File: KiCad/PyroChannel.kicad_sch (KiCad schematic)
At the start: 5 parts, among them Q3 IRLML0030

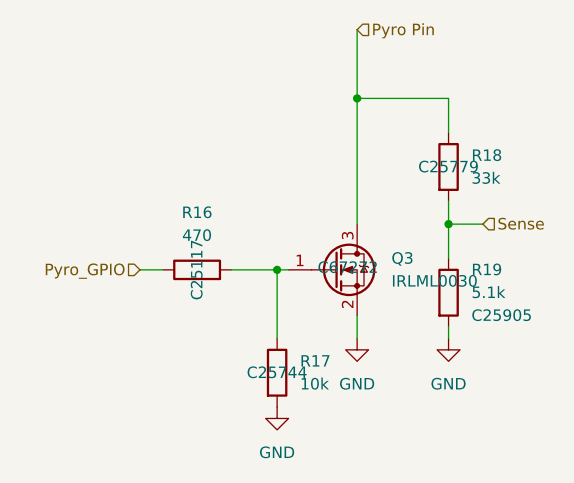
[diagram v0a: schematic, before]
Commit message: add spot for high G accelerometer
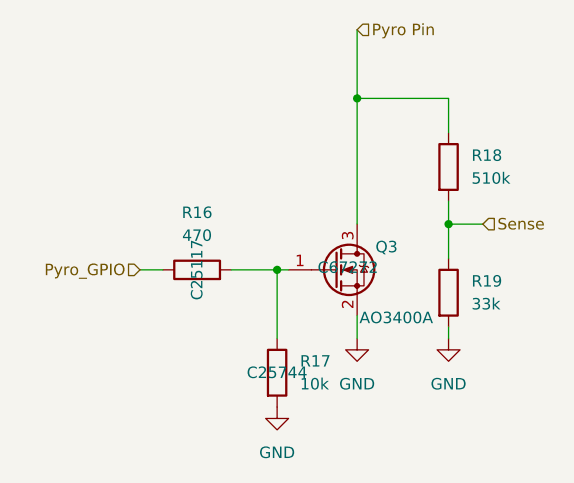
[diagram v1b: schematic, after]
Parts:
- Q3: value IRLML0030 -> AO3400A; symbol Transistor_FET:IRLML0030 -> Transistor_FET:AO3400A
- R18: value 33k -> 510k; LCSC C25779 -> C11616
- R19: value 5.1k -> 33k; LCSC C25905 -> C25779
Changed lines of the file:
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@@
 			)
 		)
-		(property "Value" "33k"
+		(property "Value" "510k"
 			(at 160.02 83.8199 0)
 			(effects
@@
 			)
 		)
-		(property "LCSC" "C25779"
+		(property "LCSC" "C11616"
 			(at 157.48 82.55 0)
 			(effects
@@
 					(size 1.27 1.27)
 				)
+				(hide yes)
 			)
 		)
@@
 	)
 	(symbol
-		(lib_id "Transistor_FET:IRLML0030")
+		(lib_id "Transistor_FET:AO3400A")
 		(at 144.78 93.98 0)
 		(unit 1)
@@
 		(dnp no)
 		(property "Reference" "Q3"
-			(at 151.13 92.7099 0)
-			(effects
-				(font
-					(size 1.27 1.27)
-				)
-				(justify left)
-			)
-		)
-		(property "Value" "IRLML0030"
-			(at 151.13 95.2499 0)
+			(at 149.352 91.44 0)
+			(effects
+				(font
+					(size 1.27 1.27)
+				)
+				(justify left)
+			)
+		)
+		(property "Value" "AO3400A"
+			(at 147.574 99.314 0)
 			(effects
 				(font
@@
 			)
 		)
-		(property "Datasheet" "https://www.infineon.com/dgdl/irlml0030pbf.pdf?fileId=5546d462533600a401535664773825df"
+		(property "Datasheet" "http://www.aosmd.com/pdfs/datasheet/AO3400A.pdf"
 			(at 149.86 97.79 0)
 			(effects
@@
 			)
 		)
-		(property "Description" "5.3A Id, 30V Vds, 27mOhm Rds, N-Channel HEXFET Power MOSFET, SOT-23"
+		(property "Description" "30V Vds, 5.7A Id, N-Channel MOSFET, SOT-23"
 			(at 144.78 93.98 0)
 			(effects
@@
 		(fields_autoplaced yes)
 		(property "Reference" "R19"
-			(at 160.02 93.9799 0)
-			(effects
-				(font
-					(size 1.27 1.27)
-				)
-				(justify left)
-			)
-		)
-		(property "Value" "5.1k"
-			(at 160.02 96.5199 0)
+			(at 160.02 95.2499 0)
+			(effects
+				(font
+					(size 1.27 1.27)
+				)
+				(justify left)
+			)
+		)
+		(property "Value" "33k"
+			(at 160.02 97.7899 0)
 			(effects
 				(font
@@
 			)
 		)
-		(property "LCSC" "C25905"
+		(property "LCSC" "C25779"
 			(at 160.02 99.0599 0)
 			(effects
@@
 				)
 				(justify left)
-			)
-		)
+				(hide yes)
+			)
+		)

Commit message: add LEDs, OSU AIAA logo
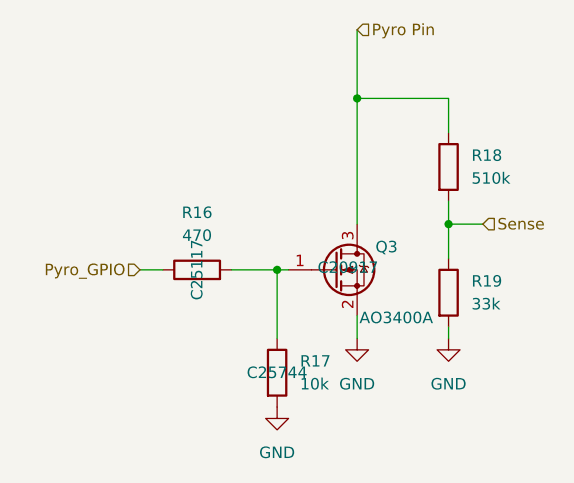
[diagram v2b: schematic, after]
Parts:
- Q3: LCSC C67272 -> C20917
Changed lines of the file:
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@@
 			)
 		)
-		(property "LCSC" "C67272"
+		(property "LCSC" "C20917"
 			(at 146.304 93.726 0)
 			(effects
